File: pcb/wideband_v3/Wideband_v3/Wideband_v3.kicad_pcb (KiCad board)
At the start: 2 copper layers, 80 x 50 mm, 75 parts, among them J1 Conn_01x10, J2 USB_C_Receptacle_USB2.0, J3 Tag connect, J4 FT_CAN, J5 Conn_01x12, Q6 MCQ9435-TP, SW1 Key0, SW3 Key1, U1 RP2040, U10 LMV358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

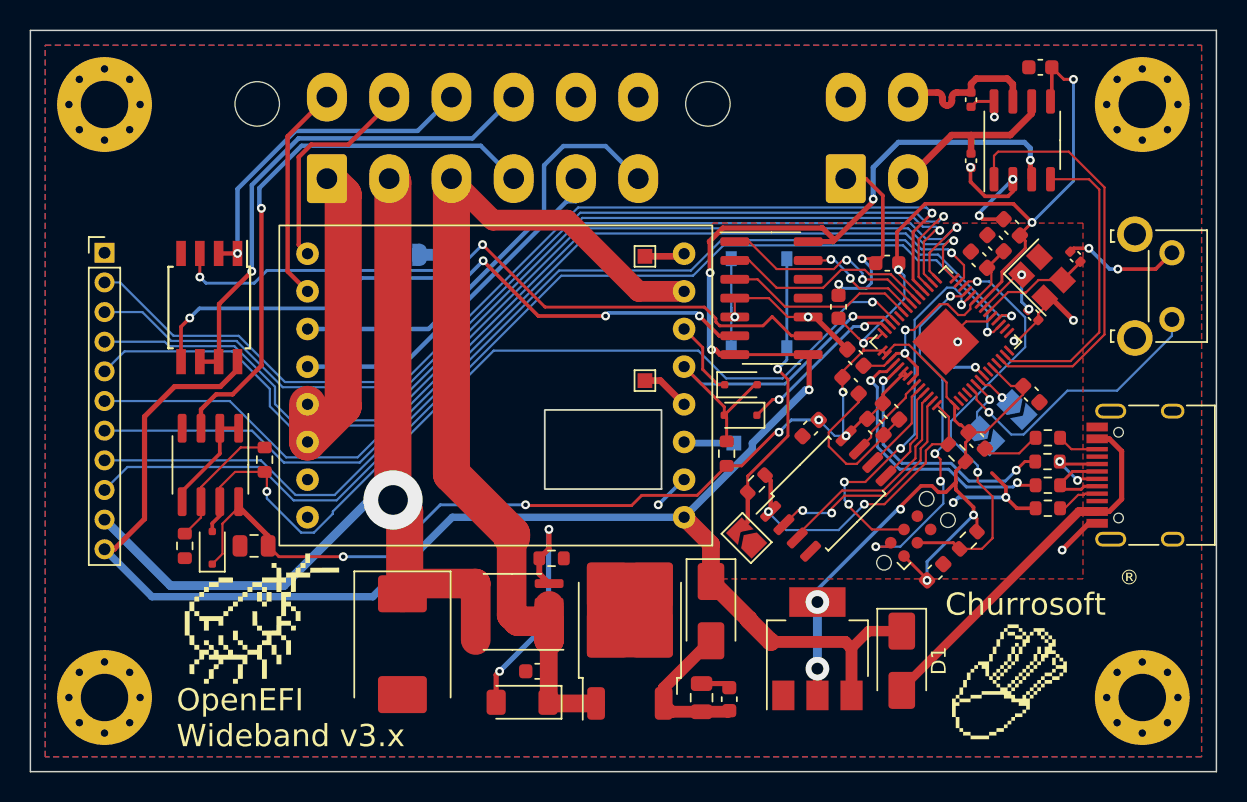
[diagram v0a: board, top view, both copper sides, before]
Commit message: rev3, reduce extended component count
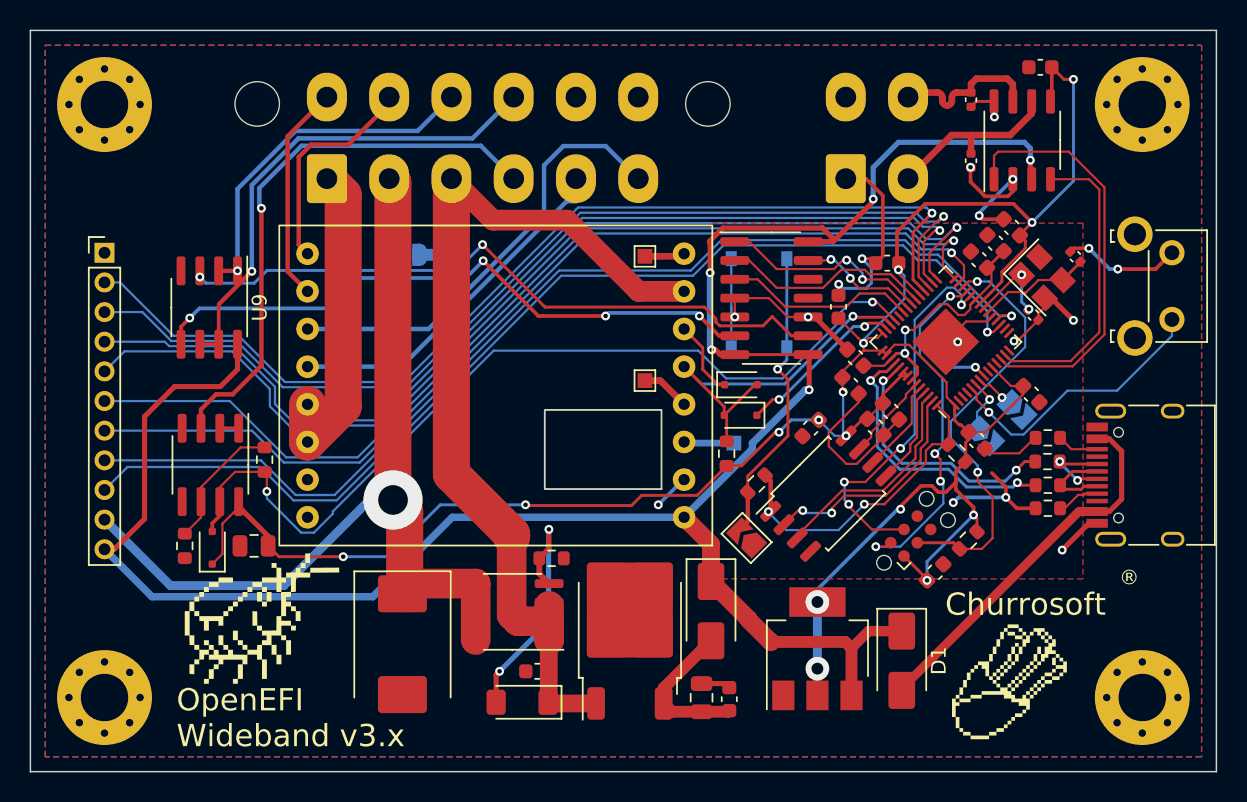
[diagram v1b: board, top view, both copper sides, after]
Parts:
- U9: footprint Package_SO:SOIC-8W_5.3x5.3mm_P1.27mm -> Package_SO:SOIC-8_3.9x4.9mm_P1.27mm
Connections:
- U10 pad 1: Net-(U10A--) -> GND
- U10 pad 2: Net-(U10A--) -> GND
- U10 pad 5: Net-(U10A--) -> GND
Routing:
- net Net-(U10A--): track 7.27 -> 0.00 mm
- net GND: track 93.4 -> 95.4 mm
- net /m_TEMP_OUT: track 47.1 -> 45.5 mm
- net +5V: track 154.8 -> 156.0 mm
- net /m_LAMBDA_OUT: track 43.8 -> 42.6 mm
- net /TEMP_OUT: track 22.6 -> 23.8 mm
- net /LAMBDA_OUT: track 34.2 -> 33.1 mm

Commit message: Optimize SKUs
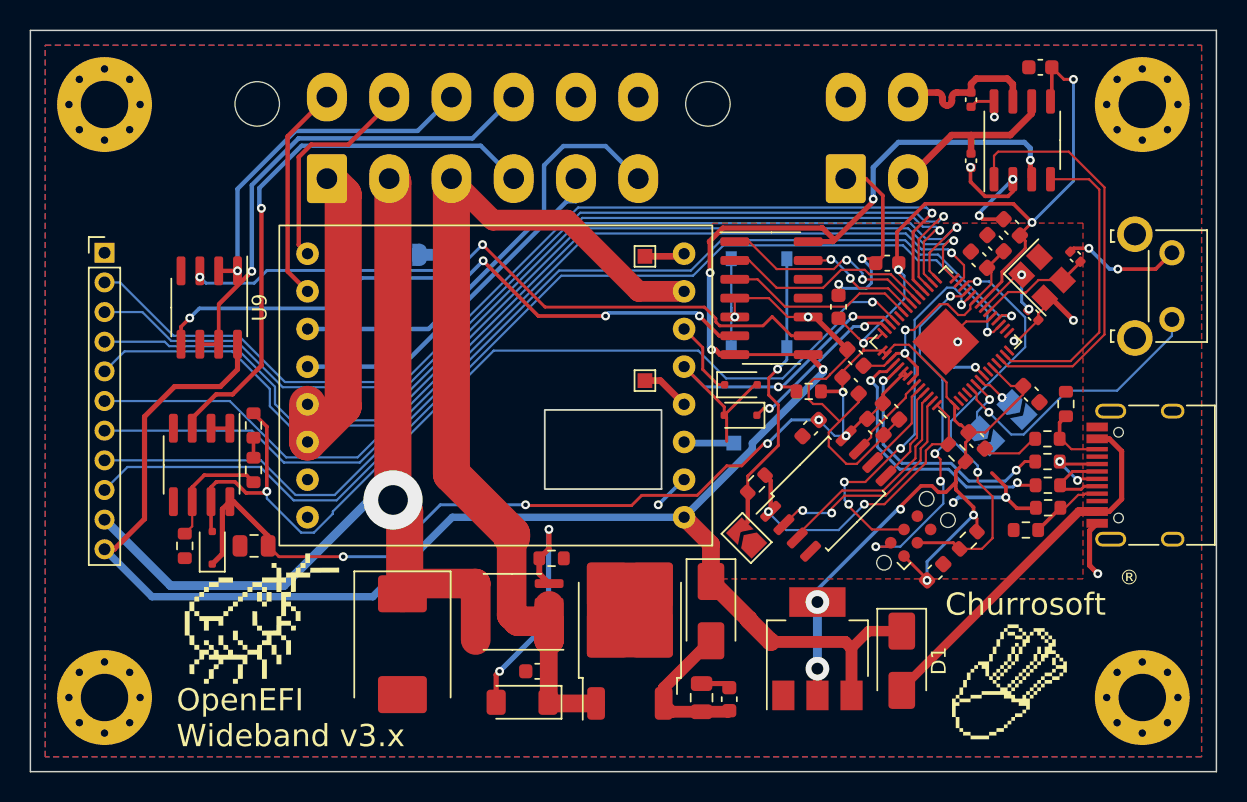
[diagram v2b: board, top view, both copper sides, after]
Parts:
- removed R1, R2: 5.1k, Resistor_SMD:R_0603_1608Metric
- removed R16: 3.3k, Resistor_SMD:R_0603_1608Metric
- removed R17: 33k, Resistor_SMD:R_0603_1608Metric
- added R10: 10k, Resistor_SMD:R_0603_1608Metric, F.Cu at (144.8, 98.8)
- added R11: 10k, Resistor_SMD:R_0603_1608Metric, F.Cu at (146.3, 97.3)
- added R12: 10k, Resistor_SMD:R_0603_1608Metric, F.Cu at (146.2, 92.7)
- added R13: 10k, Resistor_SMD:R_0603_1608Metric, F.Cu at (147.5, 90.3)
- added R7: 3k, Resistor_SMD:R_0603_1608Metric, F.Cu at (92.7, 94.8)
- added R8: 30k, Resistor_SMD:R_0603_1608Metric, F.Cu at (92.7, 91.8)
- added R9: 3k, Resistor_SMD:R_0603_1608Metric, F.Cu at (130.1, 89.5)
- moved U10 0.59 mm to (89.2, 94.4)
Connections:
- net /MCU/USB+ renamed Net-(U1-USB_DP)
- net /MCU/USB- renamed Net-(U1-USB_DM)
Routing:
- net GND: track 95.4 -> 103.1 mm
- net /m_narrow: track 61.4 -> 65.7 mm
- net Net-(J2-CC1): track 2.91 -> 5.03 mm
- net Net-(J2-CC2): track 2.82 -> 4.52 mm
- net +3V3: track 169.6 -> 171.3 mm
- net /MCU/WBO_RX: track 25.9 -> 27.4 mm, vias 1 -> 2
- net Net-(R7-Pad2): track 0.00 -> 1.35 mm
- net +5V: track 156.0 -> 156.7 mm
- net Net-(U10B--): track 8.99 -> 8.40 mm

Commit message: update DAC for v3
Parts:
- removed U7: MCP42010, Package_SO:SOIC-14_3.9x8.7mm_P1.27mm
- added U5: TPL0401A-10-Q1, Package_TO_SOT_SMD:Texas_R-PDSO-G6, F.Cu at (126.9, 81.1)
- added U6: TPL0401A-10-Q1, Package_TO_SOT_SMD:Texas_R-PDSO-G6, F.Cu at (126.9, 84.3)
- moved C17 0.13 mm to (133.0, 89.2)
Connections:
- net Net-(U1-USB_DM) renamed /MCU/USB-
- net Net-(U1-USB_DP) renamed /MCU/USB+
- U1 pad 11: /MCU/GPIO8 -> unconnected-(U1-GPIO8-Pad11)
- U1 pad 14: /MCU/GPIO11 -> unconnected-(U1-GPIO11-Pad14)
- U1 pad 15: /MCU/GPIO12 -> unconnected-(U1-GPIO12-Pad15)
- U1 pad 34: /DAC_SCK -> /DAC_SDA_1
- U1 pad 35: /DAC_CS -> /DAC_CLK_1
- U1 pad 36: /DAC_SO -> /DAC_SDA_2
- U1 pad 37: /DAC_SI -> /DAC_CLK_2
- U1 pad 38: /MCU/GPIO26 -> unconnected-(U1-GPIO26_ADC0-Pad38)
- U1 pad 9: /MCU/GPIO7 -> unconnected-(U1-GPIO7-Pad9)
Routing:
- net /DAC_CLK_2: track 0.00 -> 14.6 mm
- net /DAC_CS: track 14.4 -> 0.00 mm, vias 2 -> 0
- net /DAC_SCK: track 14.3 -> 0.00 mm
- net /DAC_SI: track 13.0 -> 0.00 mm
- net /DAC_CLK_1: track 0.00 -> 12.7 mm
- net /DAC_SDA_2: track 0.00 -> 12.4 mm
- net /DAC_SDA_1: track 0.00 -> 10.5 mm
- net /m_LAMBDA_OUT: track 42.6 -> 51.7 mm, vias 4 -> 6
- net /DAC_SO: track 8.24 -> 0.00 mm, vias 2 -> 0
- net +5V: track 156.7 -> 161.7 mm, vias 5 -> 6
- net GND: track 103.1 -> 106.2 mm, vias 17 -> 19
- net /m_TEMP_OUT: track 45.5 -> 47.6 mm, vias 2 -> 4

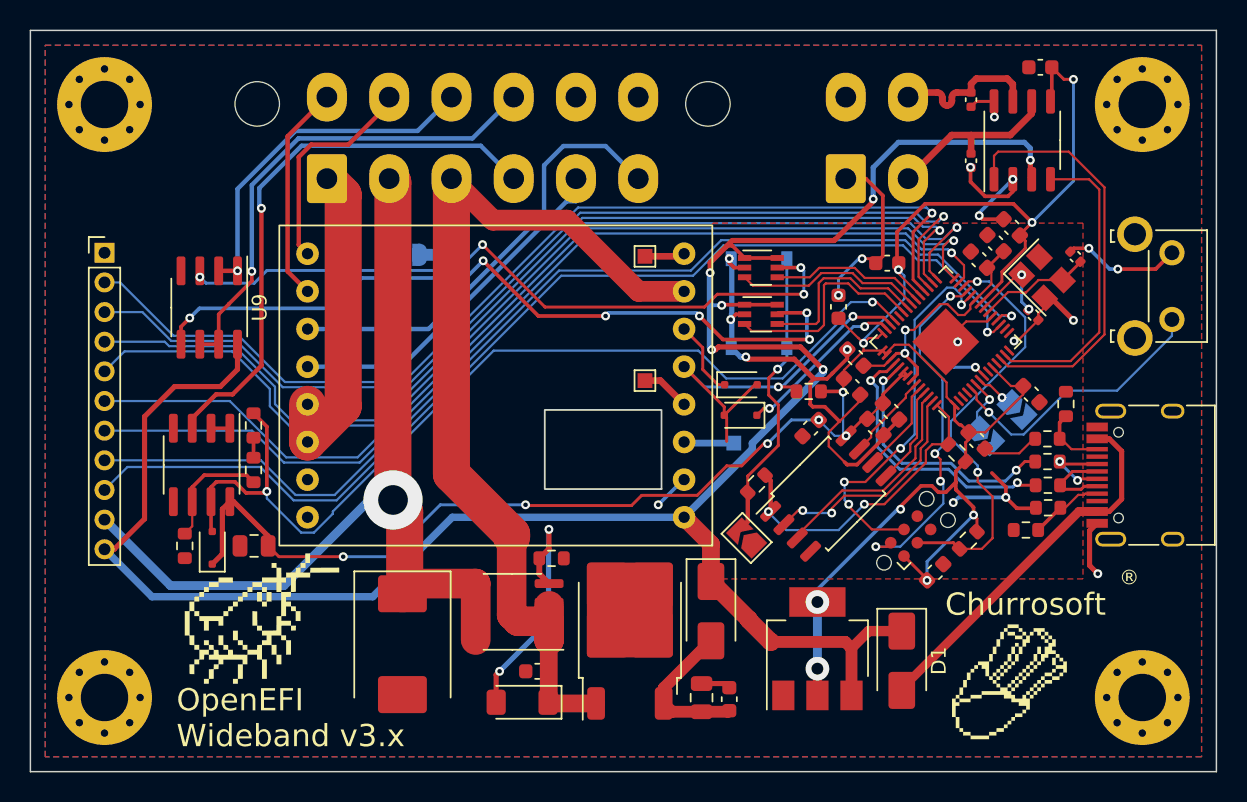
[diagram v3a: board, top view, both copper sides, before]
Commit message: rev3: update connector on main board
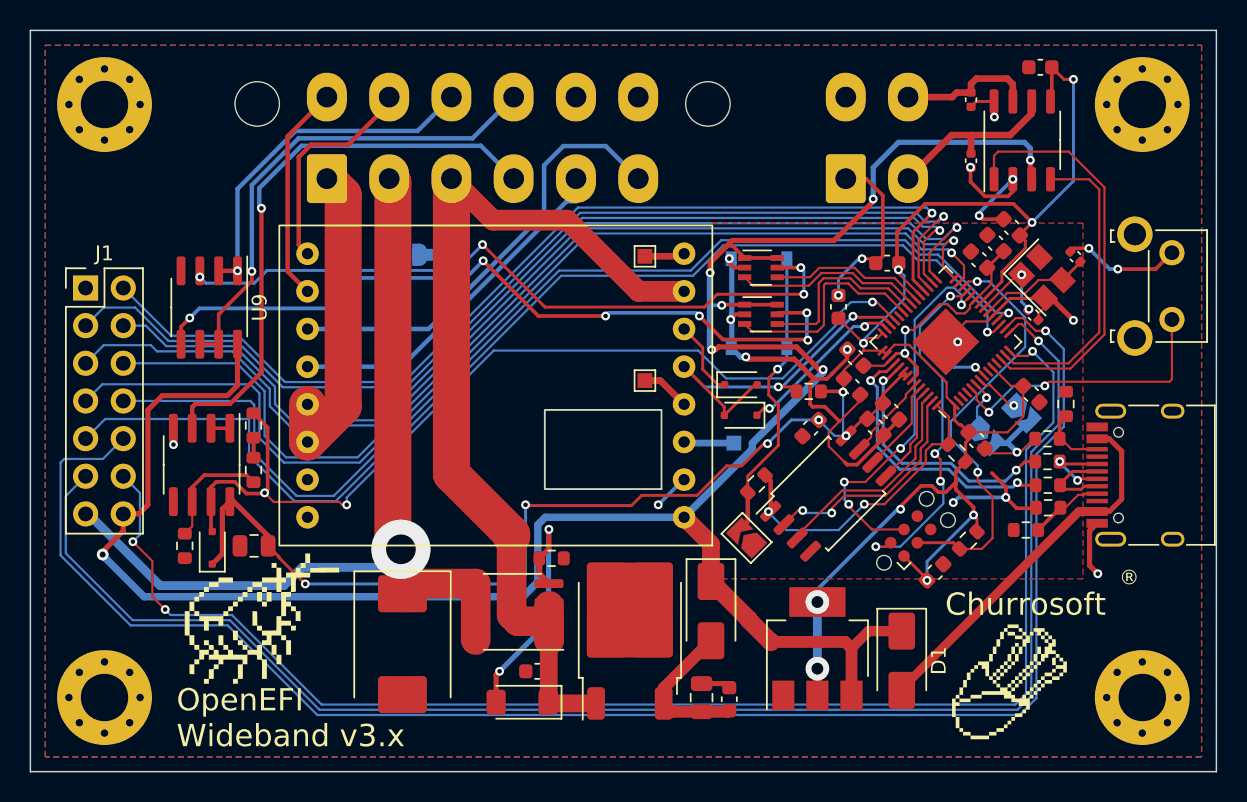
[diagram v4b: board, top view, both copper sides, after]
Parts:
- J1: value Conn_01x10 -> Conn_01x14; footprint Connector_PinHeader_2.00mm:PinHeader_1x11_P2.00mm_Vertical -> Connector_PinHeader_2.54mm:PinHeader_2x07_P2.54mm_Vertical
- moved J1 2.70 mm to (81.3, 82.5)
- moved JP2 0.38 mm to (144.5, 90.9)
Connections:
- J1 pad 10: +12VA -> /MCU/GPIO13
- J1 pad 11: +5V -> /MCU/GPIO12
- U1 pad 14: unconnected-(U1-GPIO11-Pad14) -> /MCU/GPIO11
- U1 pad 15: unconnected-(U1-GPIO12-Pad15) -> /MCU/GPIO12
- U1 pad 16: unconnected-(U1-GPIO13-Pad16) -> /MCU/GPIO13
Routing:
- net /MCU/GPIO13: track 0.00 -> 111.5 mm, vias 0 -> 1
- net /MCU/GPIO12: track 0.00 -> 103.6 mm, vias 0 -> 1
- net /MCU/GPIO11: track 0.00 -> 98.0 mm, vias 0 -> 3
- net GND: track 106.2 -> 114.2 mm, vias 19 -> 20
- net +3V3: track 171.0 -> 176.2 mm
- net /MCU/GPIO16: track 67.5 -> 72.3 mm
- net /MCU/GPIO14: track 72.6 -> 76.6 mm
- net +5V: track 161.7 -> 165.4 mm, vias 6 -> 7
- net /MCU/GPIO15: track 72.6 -> 74.5 mm
- net /MCU/GPIO20: track 69.8 -> 71.7 mm
- net /MCU/BTN_YES: track 18.9 -> 20.6 mm, vias 1 -> 2
- net /MCU/WBO_RX: track 27.4 -> 25.8 mm
- net /MCU/GPIO17: track 69.2 -> 70.7 mm
- net /m_narrow: track 65.7 -> 64.2 mm, vias 2 -> 3
- net /MCU/GPIO21: track 69.7 -> 68.3 mm
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
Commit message: Bug fixes and enhancements
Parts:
- moved G*** 22.5 mm to (120.6, 105.1)
- moved G*** 5.67 mm to (97.6, 104.1)

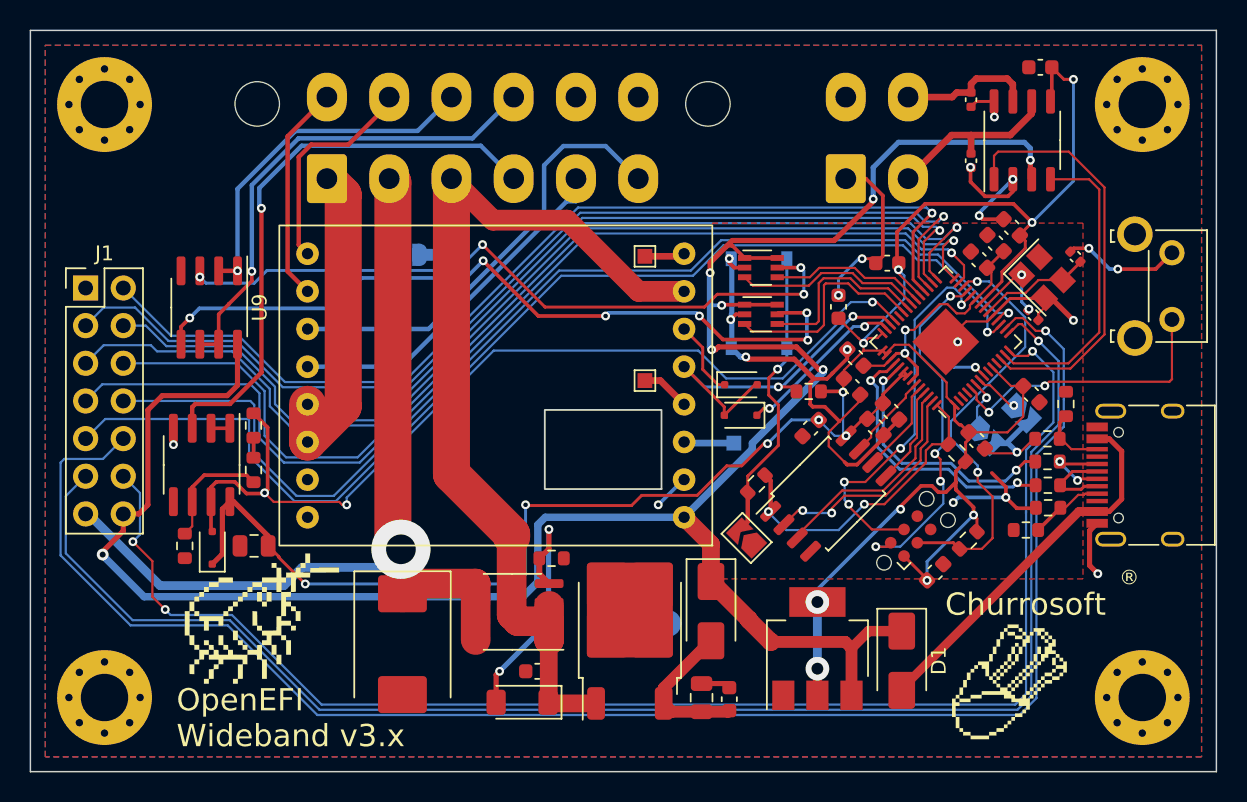
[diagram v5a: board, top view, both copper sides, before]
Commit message: update LCSC/Stock codes, update pcb to new footprints
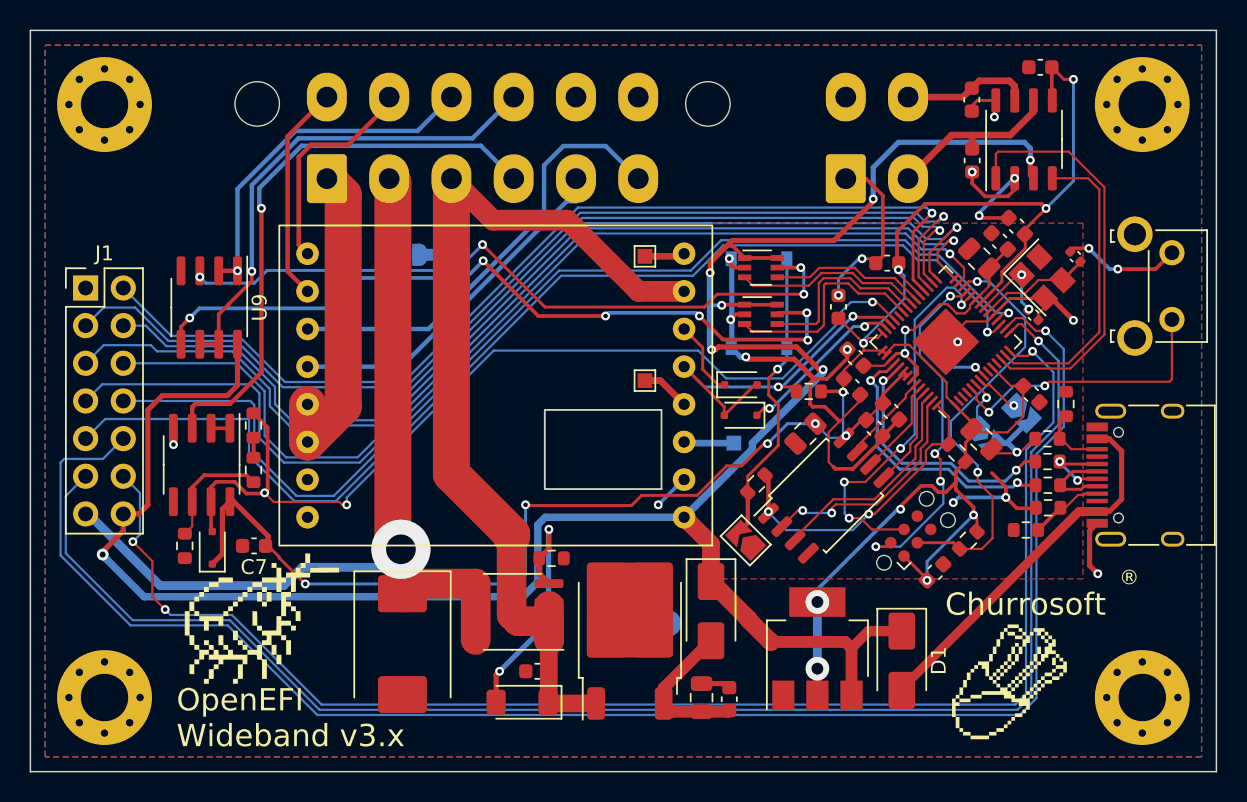
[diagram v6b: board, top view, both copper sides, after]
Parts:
- C1, C2: footprint Capacitor_SMD:C_0402_1005Metric -> Capacitor_SMD:C_0603_1608Metric
- C10, C24, C9: footprint Capacitor_SMD:C_0603_1608Metric -> Capacitor_SMD:C_0805_2012Metric
- C7: footprint Capacitor_SMD:C_0805_2012Metric -> Capacitor_SMD:C_0603_1608Metric
- D10: value D_TVS -> SMCJ24CA
- D5, D6, D7: value 1N4148W -> 1N5819WS
- moved C24 0.52 mm to (129.9, 92.3)
- moved C18 0.34 mm to (144.1, 78.3)
- moved C9 0.33 mm to (141.8, 92.7)
- moved C22 0.30 mm to (143.0, 79.4)
- moved U2 0.20 mm to (131.3, 96.5)
- moved JP4 0.17 mm to (125.9, 99.5)
- moved U4 0.14 mm to (144.6, 72.5)
- moved C11 0.11 mm to (134.5, 92.0)
- moved C2 0.08 mm to (141.1, 73.9)
- moved C10 0.07 mm to (141.6, 80.5)
- moved C1 0.05 mm to (141.1, 69.8)
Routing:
- net GND: track 114.2 -> 115.5 mm
